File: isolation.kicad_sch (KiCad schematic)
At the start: 20 parts, among them U1 UCC27517, U2 UCC27517, U3 ISO7710, U4 ISO7710, U5 DPC817

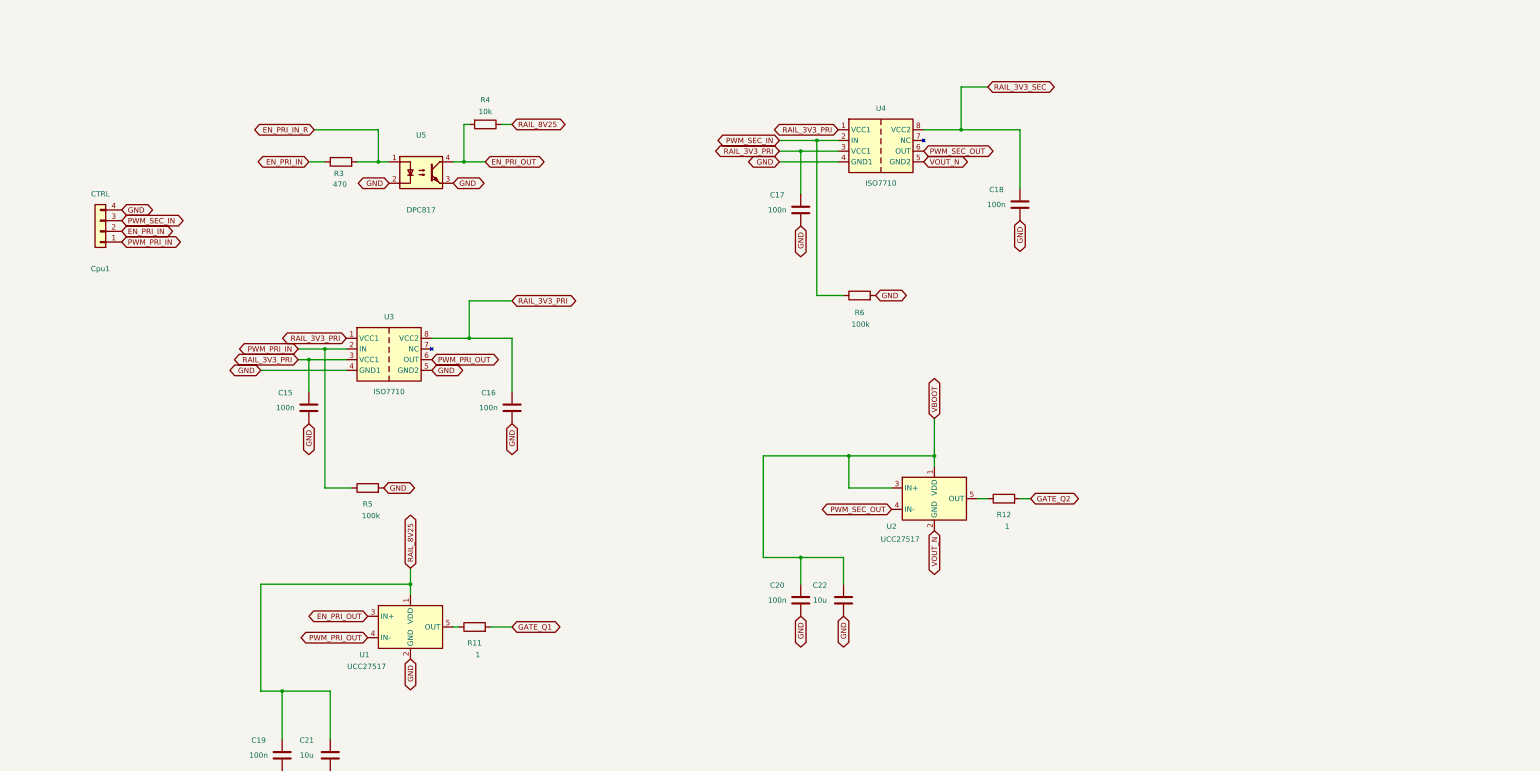
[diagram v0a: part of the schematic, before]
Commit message: Secondaire ISO7710+UCC27517 conservé, ajout retour Vout isolé AMC0311S, modèles 3D
- D2 (bootstrap) remplacé par BAT54C (cathode commune) pour compatibilité pinout
- AMC0311S (U7) ajouté : retour de mesure Vout isolé vers le connecteur C2000
- Connecteur Cpu1 étendu à 8 broches (signaux + masses)
- Correction pastilles Gate/Source sur l'empreinte custom TO-252 (pin1/pin3 inversées)
- Modèles 3D attachés aux empreintes custom (TO-252, MSD1514, A786MW V-chip)
- Image de rendu 3D ajoutée au README

Co-Authored-By: Claude Sonnet 5 <noreply@anthropic.com>
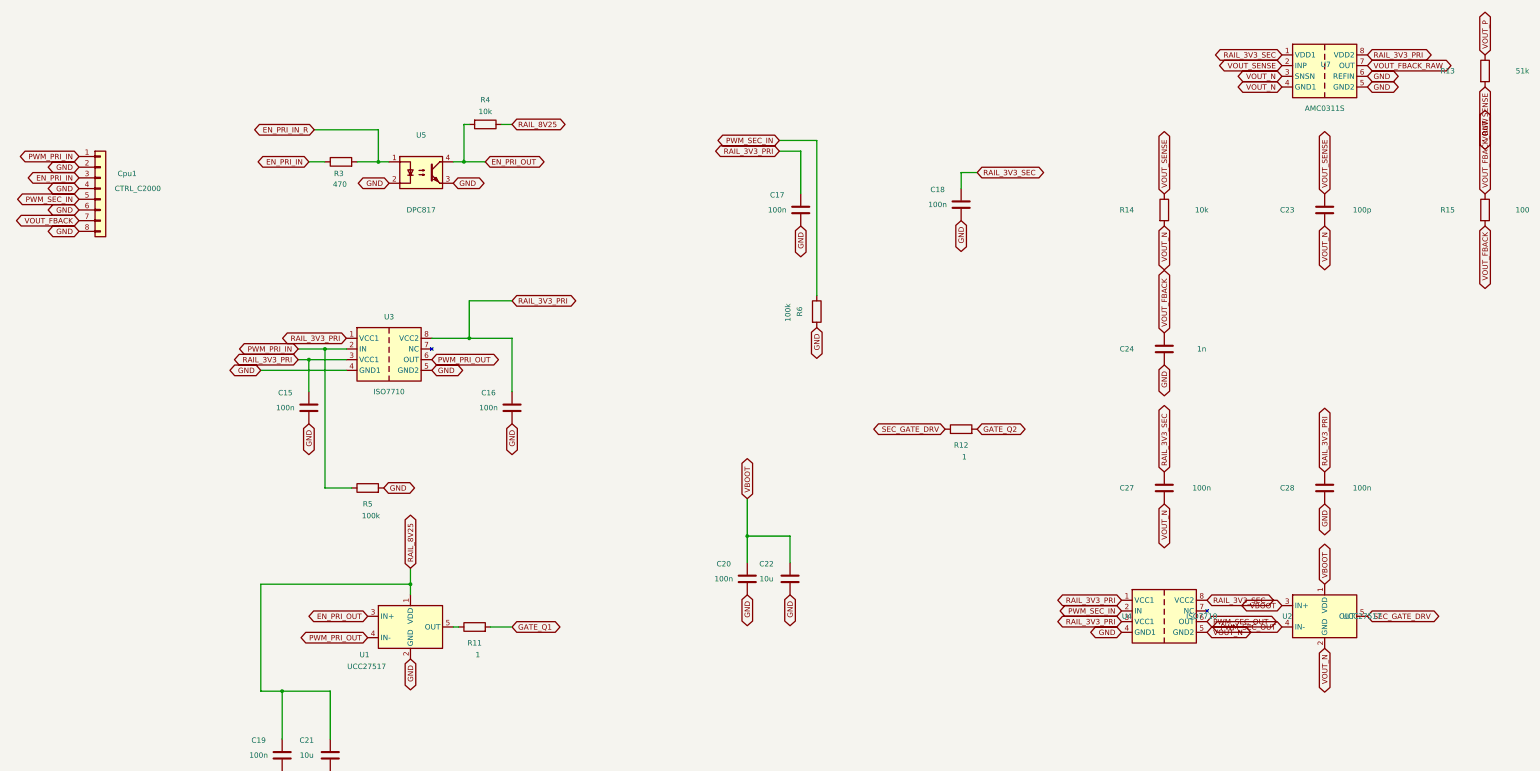
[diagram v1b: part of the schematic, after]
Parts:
- removed Cpu1: CTRL, Connector_PinHeader_2.54mm:PinHeader_1x04_P2.54mm_Vertical, symbol Connector_Generic:Conn_01x04
- added C23: 100p, Capacitor_SMD:C_0805_2012Metric, symbol Device:C
- added C24: 1n, Capacitor_SMD:C_0805_2012Metric, symbol Device:C
- added C27, C28: 100n, Capacitor_SMD:C_0805_2012Metric, symbol Device:C
- added Cpu1: CTRL_C2000, Connector_PinHeader_2.54mm:PinHeader_2x04_P2.54mm_Vertical, symbol Connector_Generic:Conn_01x08
- added R13: 51k, Resistor_SMD:R_0805_2012Metric, symbol Device:R
- added R14: 10k, Resistor_SMD:R_0805_2012Metric, symbol Device:R
- added R15: 100, Resistor_SMD:R_0805_2012Metric, symbol Device:R
- added U7: AMC0311S, Package_SO:SOIC-8_7.5x5.85mm_P1.27mm, symbol custom_parts:AMC0311S
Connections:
- net EN_PRI_IN: now also Cpu1.3 (Pin_3)
- net GND: now also C24.2, C28.2, Cpu1.2 (Pin_2), Cpu1.4 (Pin_4), Cpu1.6 (Pin_6), Cpu1.8 (Pin_8), U7.5 (GND2), U7.6 (REFIN)
- net PWM_PRI_IN: now also Cpu1.1 (Pin_1)
- net PWM_SEC_IN: now also Cpu1.5 (Pin_5)
- net RAIL_3V3_PRI: now also C28.1, U7.8 (VDD2)
- net RAIL_3V3_SEC: now also C27.1, U7.1 (VDD1)
- net VOUT_N: now also C23.2, C27.2, R14.2, U7.3 (SNSN), U7.4 (GND1)
- net SEC_GATE_DRV: now reaches R12.1, U2.5 (OUT)
- new net VOUT_FBACK: C24.1, Cpu1.7 (Pin_7), R15.2
- new net VOUT_FBACK_RAW: R15.1, U7.7 (OUT)
- new net VOUT_P: R13.1
- new net VOUT_SENSE: C23.1, R13.2, R14.1, U7.2 (INP)
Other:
- moved on the sheet: C18, C20, C22, R12, R6

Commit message: Isolation C2000 réelle (GND_CTRL/3V3_CTRL) + feuille Polarisation (HV_BIAS actif 0-90V)
- U3/U4/U5/U7/U8/U9 migrés côté contrôle vers GND_CTRL/3V3_CTRL (isolation
  du C2000 réellement effective, plus seulement nominale)
- Connecteurs CpuOut/CpuIn agrandis 2x04→2x08 (16 broches), marge pour
  futurs signaux et compatibilité avec d'autres cartes
- Nouvelle feuille polarisation.kicad_sch : pilotage actif de HV_BIAS
  (point de polarisation du secondaire flottant) depuis une alimentation
  400V externe — source de courant 300µA (BSS127I+MMBT2222), MOSFET
  variable BSS127I piloté par PWM isolé (ISO7710), protection TVS +
  pull-up grille, retour mesure isolé (AMC0311R)
- Nouveaux symboles custom BSS127I/MMBT2222, empreinte SOIC_DWV partagée
  par les amplis isolés de la famille AMC03x1R/AMC03x2R

Co-Authored-By: Claude Sonnet 5 <noreply@anthropic.com>
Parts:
- removed Cpu1: CTRL_C2000, Connector_PinHeader_2.54mm:PinHeader_2x04_P2.54mm_Vertical, symbol Connector_Generic:Conn_01x08
- added C25, C26, C31, C32: 100n, Capacitor_SMD:C_0805_2012Metric, symbol Device:C
- added C29: 100p, Capacitor_SMD:C_0805_2012Metric, symbol Device:C
- added C30, C33: 1n, Capacitor_SMD:C_0805_2012Metric, symbol Device:C
- added CpuIn: CTRL_C2000_IN, Connector_PinHeader_2.54mm:PinHeader_2x08_P2.54mm_Vertical, symbol Connector_Generic:Conn_01x16
- added CpuOut: CTRL_C2000_OUT, Connector_PinHeader_2.54mm:PinHeader_2x08_P2.54mm_Vertical, symbol Connector_Generic:Conn_01x16
- added R16: 10k, Resistor_SMD:R_0805_2012Metric, symbol Device:R
- added R17, R18: 100, Resistor_SMD:R_0805_2012Metric, symbol Device:R
- added TH1: 10k_B4000, Resistor_SMD:R_0805_2012Metric, symbol Device:Thermistor_NTC
- added U8: AMC0311R, SOIC_DWV:SOIC-8_DWV_5.85x11.5mm_P1.27mm, symbol custom_parts:AMC0311R
- added U9: AMC0302R, SOIC_DWV:SOIC-8_DWV_5.85x11.5mm_P1.27mm, symbol custom_parts:AMC0302R
- U7: value AMC0311S -> AMC0311R; footprint Package_SO:SOIC-8_7.5x5.85mm_P1.27mm -> SOIC_DWV:SOIC-8_DWV_5.85x11.5mm_P1.27mm; symbol custom_parts:AMC0311S -> custom_parts:AMC0311R
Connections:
- net EN_PRI_IN: now also CpuOut.5 (Pin_5)
- net GND: now also C25.2, C29.2, C31.2, R16.2, U8.3 (SNSN), U8.4 (GND1), U9.3 (INN), U9.4 (GND1); no longer C15.2, C17.2, C18.2, C20.2, C22.2, C24.2, C28.2, R5.2, R6.2, U3.4 (GND1), U4.4 (GND1), U5.2, U7.5 (GND2), U7.6 (REFIN)
- net PWM_PRI_IN: now also CpuOut.3 (Pin_3)
- net PWM_SEC_IN: now also CpuOut.7 (Pin_7)
- net RAIL_3V3_PRI: now also C25.1, C31.1, TH1.1, U8.1 (VDD1), U9.1 (VDD1); no longer C15.1, C17.1, C28.1, U3.1 (VCC1), U3.3 (VCC1), U4.1 (VCC1), U7.8 (VDD2)
- net VOUT_FBACK: now also CpuIn.3 (Pin_3)
- net VOUT_N: now also C18.2, C20.2, C22.2
- net EN_PRI_IN_R: no longer names the net of R3.2, U5.1
- net SEC_GATE_DRV: no longer names the net of R12.1, U2.5 (OUT)
- new net: R17.1, U8.7 (OUT)
- new net: R18.1, U9.7 (OUT)
- new net 3V3_CTRL: C15.1, C17.1, C26.1, C28.1, C32.1, CpuIn.1 (Pin_1), CpuOut.1 (Pin_1), U3.1 (VCC1), U3.3 (VCC1), U4.1 (VCC1), U7.8 (VDD2), U8.8 (VDD2), U9.8 (VDD2)
- new net BIAS_FBACK: CpuIn.9 (Pin_9)
- new net GND_CTRL: C15.2, C17.2, C24.2, C26.2, C28.2, C30.2, C32.2, C33.2, CpuIn.10 (Pin_10), CpuIn.12 (Pin_12), CpuIn.14 (Pin_14), CpuIn.16 (Pin_16), CpuIn.2 (Pin_2), CpuIn.4 (Pin_4), CpuIn.6 (Pin_6), CpuIn.8 (Pin_8), CpuOut.10 (Pin_10), CpuOut.12 (Pin_12), CpuOut.14 (Pin_14), CpuOut.16 (Pin_16), CpuOut.2 (Pin_2), CpuOut.4 (Pin_4), CpuOut.6 (Pin_6), CpuOut.8 (Pin_8), R5.2, R6.2, U3.4 (GND1), U4.4 (GND1), U5.2, U7.5 (GND2), U7.6 (REFIN), U8.5 (GND2), U8.6 (REFIN), U9.5 (GND2), U9.6 (REFIN)
- new net ISENSE_P: U9.2 (INP)
- new net ISENSE_PRI_FBACK: C33.1, CpuIn.7 (Pin_7), R18.2
- new net PWM_BIAS_IN: CpuOut.9 (Pin_9)
- new net TEMP: C29.1, R16.1, TH1.2, U8.2 (INP)
- new net TEMP_PRI_FBACK: C30.1, CpuIn.5 (Pin_5), R17.2
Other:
- moved on the sheet: C15, C16, C17, C18, C19, C20, C21, C22, C23, C24, C27, C28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

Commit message: Retours temperature/courant primaire isoles, isolation C2000 reelle, feuille Polarisation finalisee (80V, R26 corrige par simulation)
- U8 (AMC0311R) : retour temperature primaire (thermistance NTC) isole
- U9 (AMC0302R) : retour courant primaire (shunt R19) isole
- Migration GND_CTRL/3V3_CTRL : le C2000 externe recoit ses propres nets
  d'alimentation/masse isoles (U3/U4/U5/U7/U8/U9), connecteurs CpuOut/CpuIn
  agrandis a 16 broches
- Feuille polarisation.kicad_sch reprise en etiquettes globales uniquement
  (plus de fils explicites) et alignee sur la grille 1.27mm
- Source de courant Q3/Q4/R25/R26 simplifiee a un rail fixe 80V (HV80_IN,
  ex-400V) ; R26 corrige de 2M7 a 75k apres simulation SPICE (ngspice,
  modeles reels Diodes Inc.) qui a revele que le montage se comporte
  comme une resistance plutot qu'une source plate - voir 00-intention-
  conception.md §15bis
- Nouveau script bom_family_report.py (remplace BOMconverter.py) :
  nomenclature groupee par famille, sans dependance externe, lit soit le
  netlist XML legacy d'Eeschema soit un CSV kicad-cli
- README.md : image du schema integree
- Mise a jour 00-intention-conception.md (§13-15bis)

Co-Authored-By: Claude Sonnet 5 <noreply@anthropic.com>
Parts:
- renumbered CpuIn to CpuIn1, CpuOut to CpuOut1
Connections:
- net 3V3_CTRL: now also U4.3 (VCC1)
- net RAIL_3V3_PRI: no longer U4.3 (VCC1)
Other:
- moved on the sheet: C15, C16, C17, C20, C22, C23, C25, C26, C27, C29, C30, CpuIn1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

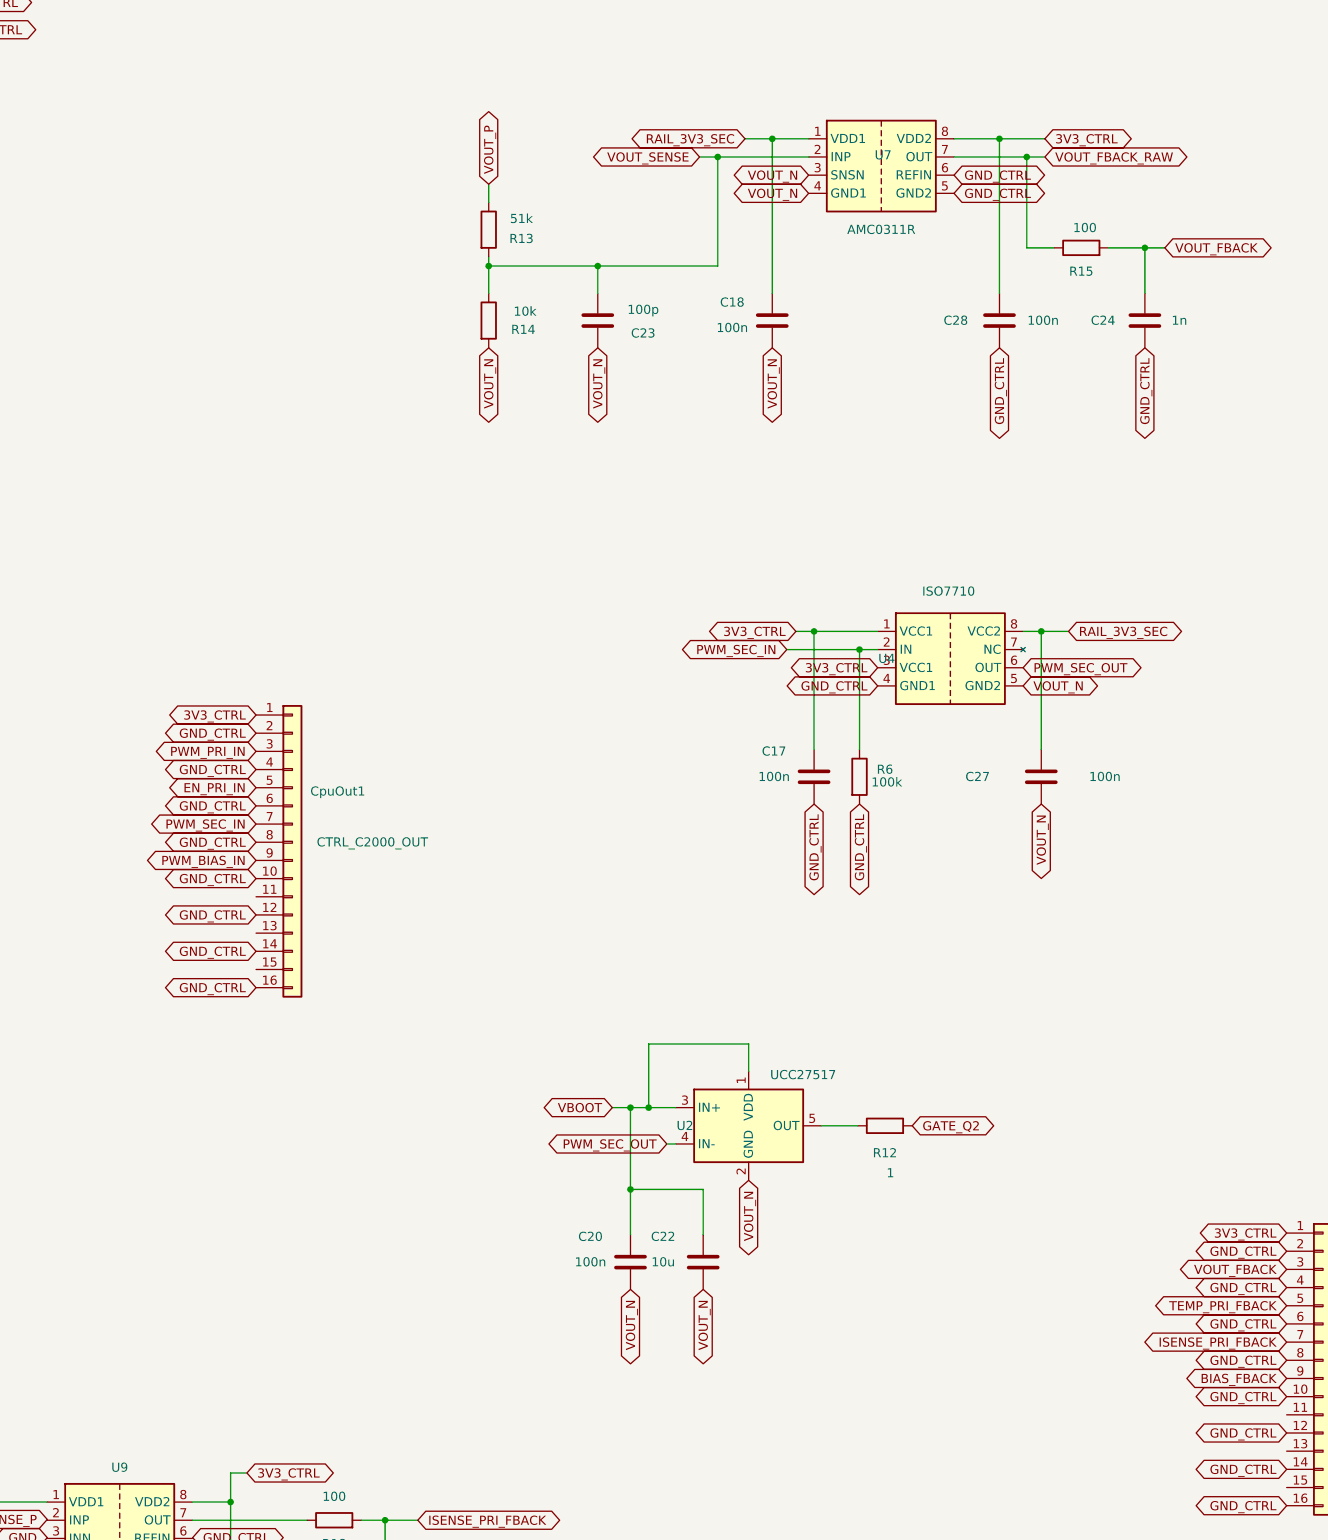
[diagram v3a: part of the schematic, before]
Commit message: Validation 18,9W + redressement synchrone : UCC24612 (U12) remplace U2/U4, clamp D4 ajouté
Simulation SPICE à la cible réelle (18,9W, pas les 10W de validation initiale) :
Vds_Q2 dépasse 100V dès Vin=20V sans clamp secondaire, indépendamment du
redresseur. UCC24612 amène +5pts de rendement mais ne corrige pas la
surtension -- D4 (SMCJ54A) ajouté pour ça. U2/U4 retirés (timing firmware
aveugle, remplacé par la détection Vds de l'UCC24612).

Co-Authored-By: Claude Sonnet 5 <noreply@anthropic.com>
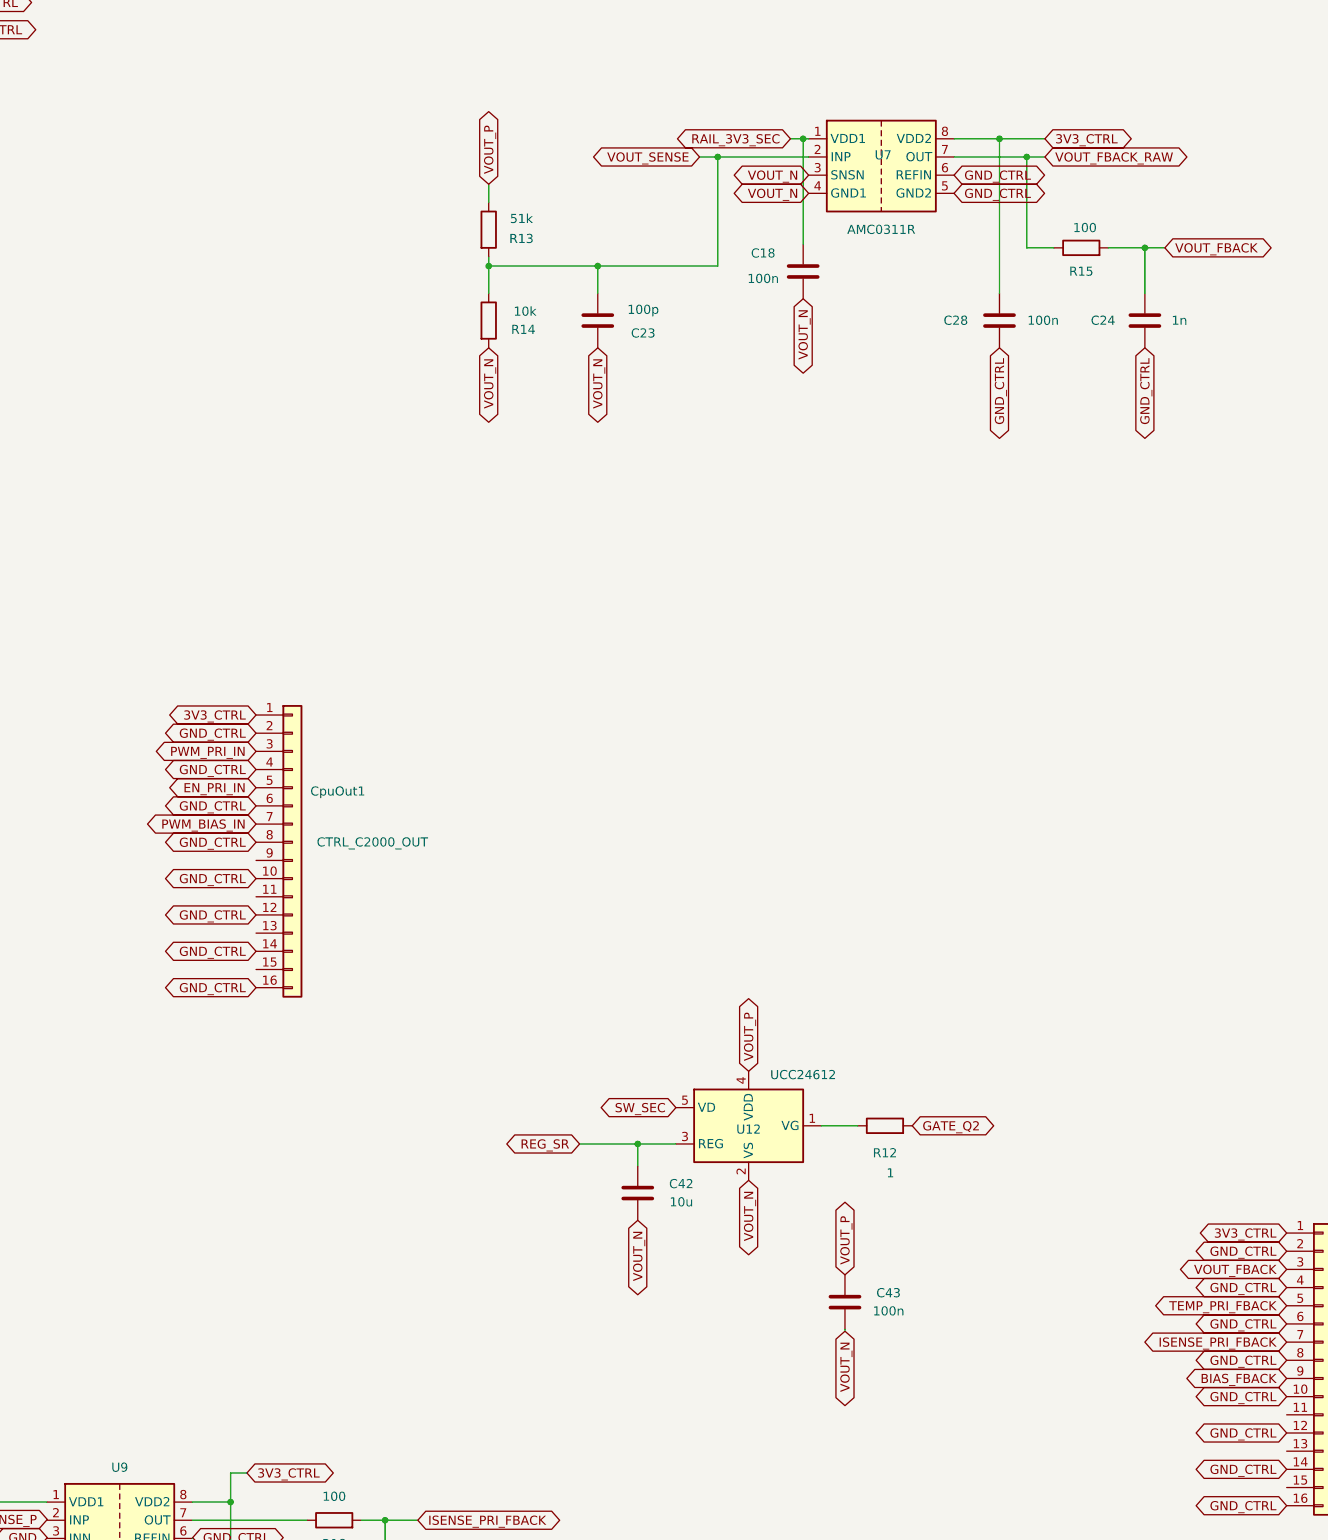
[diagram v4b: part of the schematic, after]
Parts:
- removed C17, C20, C27: 100n, Capacitor_SMD:C_0805_2012Metric, symbol Device:C
- removed C22: 10u, Capacitor_SMD:C_0805_2012Metric, symbol Device:C
- removed R6: 100k, Resistor_SMD:R_0805_2012Metric, symbol Device:R
- removed U2: UCC27517, Package_TO_SOT_SMD:SOT-23-5, symbol custom_parts:UCC27517
- removed U4: ISO7710, Package_SO:SOIC-8_3.9x4.9mm_P1.27mm, symbol custom_parts:ISO7710
- added C42: 10u, Capacitor_SMD:C_0805_2012Metric, symbol Device:C
- added C43: 100n, Capacitor_SMD:C_0805_2012Metric, symbol Device:C
- added U12: UCC24612, Package_TO_SOT_SMD:SOT-23-5, symbol custom_parts:UCC24612
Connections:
- net PWM_SEC_IN is gone; now on net PWM_BIAS_IN: CpuOut1.7 (Pin_7)
- net PWM_BIAS_IN: no longer CpuOut1.9 (Pin_9)
- net VOUT_N: now also C42.1, C43.1, U12.2 (VS)
- net VOUT_P: now also C43.2, U12.4 (VDD)
- net at R12.1: now also U12.1 (VG)
- new net REG_SR: C42.2, U12.3 (REG)
- new net SW_SEC: U12.5 (VD)
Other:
- moved on the sheet: C18
